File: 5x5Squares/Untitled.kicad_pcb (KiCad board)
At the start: 2 copper layers, 297 x 289.2 mm, 85 parts

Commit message: updated 5x5 square board based on Miguel's feedback
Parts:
- added G***: LOGO, Symbol:consortium_logo_5cm, F.Cu at (311.7, 303.2)
- added G***: LOGO, Symbol:UCR_Logo_3cm, F.Cu at (256.1, 305.0)
- added G***: LOGO, Symbol:ZDC_logo_20x20cm, B.Cu at (164.7, 164.9)
- G***: footprint Symbol:ZDC_logo -> Symbol:ZDC_logo_20x20mm; moved to F.Cu
- G***: footprint Symbol:consortium_logo_3cm -> Symbol:Consortium_logo_11cm
- G***: footprint Symbol:UCR_Logo_3cm -> Symbol:UCR_logo_10cm
- moved G*** 130.6 mm to (210.3, 305.7), turned to 0 degrees
- moved G*** 59.8 mm to (295.6, 77.2)
- moved G*** 15.6 mm to (283.5, 175.2)
- moved G*** 12.1 mm to (55.0, 294.9)
- moved G*** 7.50 mm to (54.7, 284.6)
- moved 10 nF 1.81 mm to (64.5, 47.9)
- moved 10 nF 1.72 mm to (65.4, 161.7)
- moved 10 nF 0.90 mm to (65.3, 54.3)
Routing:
- net (no net): track 12318.6 -> 12314.6 mm, vias 158 -> 157
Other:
- outline, holes or cut-outs redrawn
- board text added: "Note: board does not extend all the way to the edge of the absorbers due to limitations on board size"
- board text added: "SiPM size: 1.3 mm space between SiPMs: 47.8 mm Absorber area: ~30x30 cm (3x3 blocks) Rotate every other board by 180 degrees for S2 staggering."

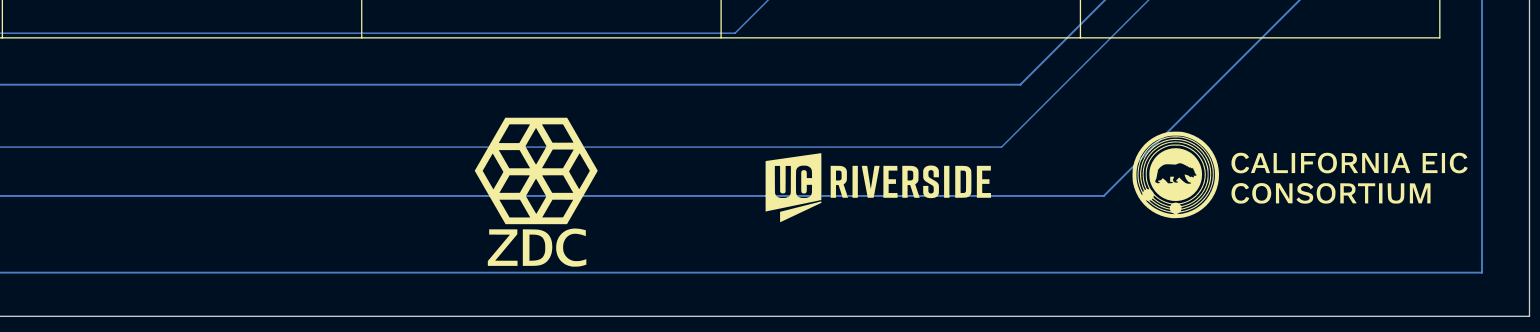
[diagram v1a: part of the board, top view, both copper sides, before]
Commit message: updated 5x5 square board; added ePIC logo
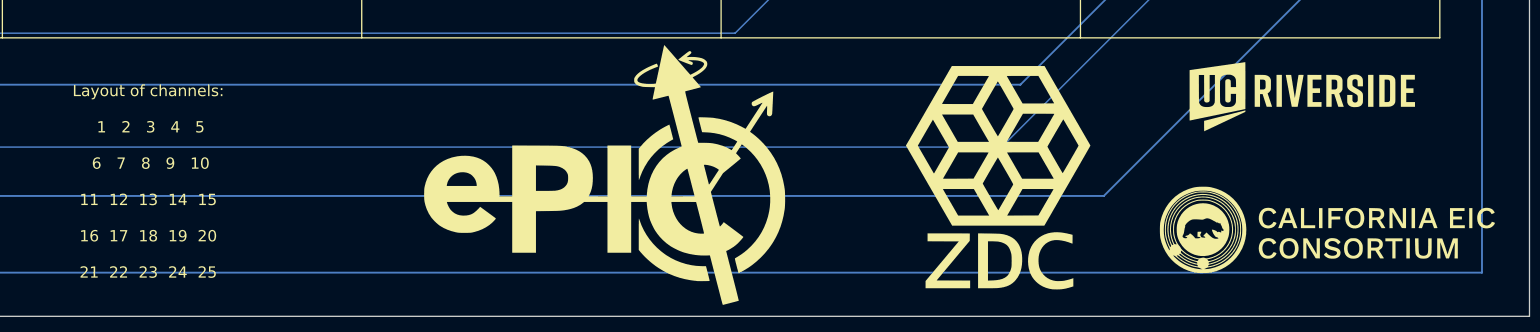
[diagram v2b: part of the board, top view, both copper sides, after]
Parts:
- added G***: LOGO, Symbol:ePIC_logo_5.0cm, F.Cu at (219.7, 303.3)
- added G***: LOGO, Symbol:ePIC_logo_6.8cm, B.Cu at (280.7, 236.2)
- G***: footprint Symbol:ZDC_logo_20x20mm -> Symbol:ZDC_logo_30x30mm
- moved G*** 61.3 mm to (271.6, 303.8)
- moved G*** 57.7 mm to (312.5, 292.9)
- moved G*** 8.18 mm to (315.3, 310.5)
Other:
- board text added: "Layout of channels: 1 2 3 4 5 6 7 8 9 10 11 12 13 14 15 16 17 18 19 20 21 22 23 24 25"

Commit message: updated 5x5 square board; added dimensions
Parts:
- moved G*** 17.1 mm to (278.5, 76.9)
- moved G*** 10.3 mm to (54.5, 294.9)
- moved G*** 6.70 mm to (54.9, 301.6)
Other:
- board text added: "SiPM size: 1.3 mm space between SiPMs: 47.8 mm Absorber area: ~30x30 cm (3x3 blocks) Rotate every other board by 180 degrees for S2 staggering. Hole positions (relative to UL corner, mm): (24.28, 17.05) (24.28, 132.65) (24.28, 248.25) Hole radii are all 1.6 mm"
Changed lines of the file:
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@@
   )
   (footprint "Symbol:UCR_logo_1.4cm" (layer "F.Cu")
-    (at 54.7 284.6)
+    (at 54.5 294.9)
     (attr board_only exclude_from_pos_files exclude_from_bom)
     (fp_text reference "G***" (at 0 0) (layer "F.SilkS") hide
@@
   )
   (footprint "Symbol:Consortium_logo_1pt4cm" (layer "F.Cu")
-    (at 55 294.9)
+    (at 54.9 301.6)
     (attr board_only exclude_from_pos_files exclude_from_bom)
     (fp_text reference "G***" (at 0 0) (layer "F.SilkS") hide
@@
   )
   (footprint "Symbol:UCR_logo_10cm" (layer "B.Cu")
-    (at 295.6 77.2 180)
+    (at 278.5 76.9 180)
     (attr board_only exclude_from_pos_files exclude_from_bom)
     (fp_text reference "G***" (at 0 0) (layer "B.SilkS") hide
@@
   (gr_line (start 91.79 93.87) (end 330.79 93.87) (layer "F.SilkS") (width 0.15))
   (gr_line (start 91.79 46.07) (end 330.79 46.07) (layer "F.SilkS") (width 0.15))
+  (gr_line (start 74.24 32.92) (end 74.24 53.4) (layer "F.SilkS") (width 0.15))
   (gr_line (start 220.24 177.51) (end 223.24 177.51) (layer "F.SilkS") (width 0.1))
   (gr_circle (center 70 281.16) (end 71.6 281.16) (layer "Edge.Cuts") (width 0.1) (fill none))
@@
     (effects (font (size 5 5) (thickness 0.15)))
   )
-  (gr_text "Layout of channels:\n\n 1   2   3   4   5 \n\n 6   7   8   9   10\n\n11  12  13  14  15\n\n16  17  18  19  20\n\n21  22  23  24  25" (at 159 304.2) (layer "F.SilkS")
+  (gr_text "Layout of channels:\n\n 1   2   3   4   5 \n\n 6   7   8   9   10\n\n11  12  13  14  15\n\n16  17  18  19  20\n\n21  22  23  24  25" (at 149.3 304.1) (layer "F.SilkS")
     (effects (font (size 1.5 1.5) (thickness 0.15)))
   )
@@
     (effects (font (size 1 1) (thickness 0.15)))
   )
-  (gr_text "This line aligns with the edge of the absorbers" (at 72.2 287.6 270) (layer "F.SilkS")
+  (gr_text "This line aligns with the edge of the absorbers" (at 72.3 254.9 270) (layer "F.SilkS")
     (effects (font (size 1 1) (thickness 0.15)))
   )
@@
     (effects (font (size 5 5) (thickness 0.15)))
   )
-  (gr_text "SiPM size: 1.3 mm\nspace between SiPMs:  47.8 mm\nAbsorber area:   ~30x30 cm (3x3 blocks)\n\nRotate every other board by \n180 degrees for S2 staggering. " (at 84.6 300.6) (layer "F.SilkS")
+  (gr_text "SiPM size: 1.3 mm\nspace between SiPMs:  47.8 mm\nAbsorber area:   ~30x30 cm (3x3 blocks)\n\nRotate every other board by \n180 degrees for S2 staggering. \n\nHole positions (relative to UL corner, mm):\n(24.28, 17.05)\n(24.28, 132.65)\n(24.28, 248.25)\nHole radii are all 1.6 mm" (at 82.1 304.1) (layer "F.SilkS")
     (effects (font (size 1.5 1.5) (thickness 0.15)) (justify left))
   )
@@
     (effects (font (size 1 1) (thickness 0.15)))
   )
-  (gr_text "Designed by \nSebouh J Paul\nVersion 1\n" (at 55.2 274.5) (layer "F.SilkS")
+  (gr_text "Designed by \nSebouh J Paul\nVersion 1\n" (at 55.2 287.9) (layer "F.SilkS")
     (effects (font (size 1.5 1.5) (thickness 0.3)))
   )
@@
     (effects (font (size 1 1) (thickness 0.15)))
   )
+  (dimension (type aligned) (layer "F.SilkS")
+    (pts (xy 91.79 46.07) (xy 330.79 46.07))
+    (height -1.97)
+    (gr_text "239.00 mm" (at 211.29 42.95) (layer "F.SilkS")
+      (effects (font (size 1 1) (thickness 0.15)))
+    )
+    (format (units 3) (units_format 1) (precision 2))
+    (style (thickness 0.05) (arrow_length 1.27) (text_position_mode 0) (extension_height 0.58642) (extension_offset 0.5) keep_text_aligned)
+  )
+  (dimension (type aligned) (layer "F.SilkS")
+    (pts (xy 91.79 46.07) (xy 91.79 285.07))
+    (height 5.09)
+    (gr_text "239.00 mm" (at 85.6 165.57 90) (layer "F.SilkS")
+      (effects (font (size 1 1) (thickness 0.1)))
+    )
+    (format (units 3) (units_format 1) (precision 2))
+    (style (thickness 0.05) (arrow_length 1.27) (text_position_mode 0) (extension_height 0.58642) (extension_offset 0.5) keep_text_aligned)
+  )
+  (dimension (type aligned) (layer "F.SilkS")
+    (pts (xy 91.79 93.87) (xy 74.24 93.87))
+    (height 3.069999)
+    (gr_text "17.55 mm" (at 81.4 89.5) (layer "F.SilkS")
+      (effects (font (size 1 1) (thickness 0.15)))
+    )
+    (format (units 3) (units_format 1) (precision 2))
+    (style (thickness 0.05) (arrow_length 1.27) (text_position_mode 2) (extension_height 0.58642) (extension_offset 0.5) keep_text_aligned)
+  )
+  (dimension (type aligned) (layer "F.SilkS")
+    (pts (xy 139.59 46.07) (xy 139.59 32.91))
+    (height 4.11)
+    (gr_text "13.16 mm" (at 142.2 38.7 90) (layer "F.SilkS")
+      (effects (font (size 1 1) (thickness 0.15)))
+    )
+    (format (units 3) (units_format 1) (precision 2))
+    (style (thickness 0.05) (arrow_length 1.27) (text_position_mode 2) (extension_height 0.58642) (extension_offset 0.5) keep_text_aligned)
+  )
+  (dimension (type aligned) (layer "F.SilkS")
+    (pts (xy 187.39 285.07) (xy 187.39 322.11))
+    (height 2.29)
+    (gr_text "37.04 mm" (at 183.95 303.59 90) (layer "F.SilkS")
+      (effects (font (size 1 1) (thickness 0.15)))
+    )
+    (format (units 3) (units_format 1) (precision 2))
+    (style (thickness 0.05) (arrow_length 1.27) (text_position_mode 0) (extension_height 0.58642) (extension_offset 0.5) keep_text_aligned)
+  )
+  (dimension (type aligned) (layer "F.SilkS")
+    (pts (xy 45.72 322.11) (xy 74.24 322.11))
+    (height -42.91)
+    (gr_text "28.52 mm" (at 59.98 278.05) (layer "F.SilkS")
+      (effects (font (size 1 1) (thickness 0.15)))
+    )
+    (format (units 3) (units_format 1) (precision 2))
+    (style (thickness 0.05) (arrow_length 1.27) (text_position_mode 0) (extension_height 0.58642) (extension_offset 0.5) keep_text_aligned)
+  )
+  (dimension (type aligned) (layer "F.SilkS")
+    (pts (xy 45.72 32.91) (xy 342.72 32.91))
+    (height 242.69)
+    (gr_text "297.00 mm" (at 194.22 274.45) (layer "F.SilkS")
+      (effects (font (size 1 1) (thickness 0.15)))
+    )
+    (format (units 3) (units_format 1) (precision 2))
+    (style (thickness 0.05) (arrow_length 1.27) (text_position_mode 0) (extension_height 0.58642) (extension_offset 0.5) keep_text_aligned)
+  )
+  (dimension (type aligned) (layer "F.SilkS")
+    (pts (xy 342.72 285.07) (xy 330.79 285.07))
+    (height 5.07)
+    (gr_text "11.93 mm" (at 336.755 278.85) (layer "F.SilkS")
+      (effects (font (size 1 1) (thickness 0.15)))
+    )
+    (format (units 3) (units_format 1) (precision 2))
+    (style (thickness 0.05) (arrow_length 1.27) (text_position_mode 0) (extension_height 0.58642) (extension_offset 0.5) keep_text_aligned)
+  )
+  (dimension (type aligned) (layer "F.SilkS")
+    (pts (xy 342.72 32.91) (xy 342.72 322.11))
+    (height 7.62)
+    (gr_text "289.20 mm" (at 333.95 177.51 90) (layer "F.SilkS")
+      (effects (font (size 1 1) (thickness 0.15)))
+    )
+    (format (units 3) (units_format 1) (precision 2))
+    (style (thickness 0.05) (arrow_length 1.27) (text_position_mode 0) (extension_height 0.58642) (extension_offset 0.5) keep_text_aligned)
+  )
   (segment (start 210.0175 261.66) (end 209.04 261.66) (width 0.2) (layer "F.Cu") (net 0))

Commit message: added dimensions; thicker lines for grid to distinguish from dimensions
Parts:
- removed the G*** at (54.5, 294.9)
- removed the G*** at (54.9, 301.6)
- moved G*** 256.2 mm to (302.5, 36.9)
- moved G*** 255.3 mm to (232.5, 48.3)
- moved G*** 253.7 mm to (273.6, 50.1)
- moved G*** 253.2 mm to (308.2, 57.4)
- moved G*** 182.4 mm to (152.8, 48.0)
- moved G*** 152.1 mm to (141.8, 298.1)
- moved G*** 68.6 mm to (232.4, 176.2)
- moved G*** 32.9 mm to (298.2, 50.5)
- moved REF** 28.2 mm to (130.6, 93.9)
- moved REF**10 28.2 mm to (130.6, 189.5)
- moved REF**12 28.2 mm to (226.2, 189.5)
- moved REF**13 28.2 mm to (274.0, 189.5)
- moved REF**14 28.2 mm to (321.8, 189.5)
- moved REF**2 28.2 mm to (226.2, 93.9)
- moved REF**3 28.2 mm to (274.0, 93.9)
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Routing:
- net (no net): track 12314.6 -> 13706.2 mm
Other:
- board size 297 x 289.2 mm -> 300 x 300 mm
- board text added: "1 mm from active area to edge"
- board text added: "Designed by Sebouh J Paul Version 2"
- board text added: "SiPM size: 1.3 mm space between SiPMs: 47.8 mm Absorber area: ~30x30 cm (3x3 blocks) Rotate every other board by 180 degrees along x axis and shift horizontally for S2 staggering. Hole positions (relative to UL corner, mm): (23.28, 40.95) (23.28, 156.55) (23.28, 272.15) Hole radii are all 1.6 mm"
- board text added: "SiPM size: 1.3 mm space between SiPMs: 47.8 mm Absorber area: ~30x30 cm (3x3 blocks) Rotate every other board by 180 degrees along x axis, and offset horizontally for S2 staggering."
- board text added: "This line aligns with the edge of the absorbers (even layers)"
- board text added: "This line aligns with the edge of the absorbers (odd layers)"
- board text removed: "Designed by Sebouh J Paul Version 1"
- board text removed: "Note: board does not extend all the way to the edge of the absorbers due to limitations on board size"
- board text removed: "SiPM size: 1.3 mm space between SiPMs: 47.8 mm Absorber area: ~30x30 cm (3x3 blocks) Rotate every other board by 180 degrees for S2 staggering."
- board text removed: "SiPM size: 1.3 mm space between SiPMs: 47.8 mm Absorber area: ~30x30 cm (3x3 blocks) Rotate every other board by 180 degrees for S2 staggering. Hole positions (relative to UL corner, mm): (24.28, 17.05) (24.28, 132.65) (24.28, 248.25) Hole radii are all 1.6 mm"
- board text removed: "This line aligns with the edge of the absorbers"
